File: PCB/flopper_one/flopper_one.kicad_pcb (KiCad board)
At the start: 2 copper layers, 76.8 x 63 mm, 23 parts, among them J1 To PN532 ->, J2 <- ST7789, Q1 2N2219, SW1 SW_Omron_B3FS, SW2 SW_Omron_B3FS, SW3 SW_Omron_B3FS, SW4 SW_Omron_B3FS, SW5 SW_Omron_B3FS, SW6 SW_SPST, U1 TP4056-42-ESOP8, U4 hw-045

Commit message: "quick" schematic fix
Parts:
- added R6: 0.4Ω, Resistor_THT:R_Axial_DIN0207_L6.3mm_D2.5mm_P7.62mm_Horizontal, F.Cu at (98.4, 33.5)
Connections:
- C2 pad 1: /VIN -> Net-(D2-A)
- D2 pad 2: GND -> Net-(D2-A)
- D3 pad 2: GND -> Net-(D2-A)
- U1 pad 4: /VIN -> Net-(D2-A)
- U1 pad 8: /VIN -> Net-(D2-A)
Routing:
- net Net-(D2-A): track 0.00 -> 100.2 mm, vias 0 -> 2
- net /VIN: track 71.0 -> 96.0 mm, vias 2 -> 3
- net GND: track 355.4 -> 343.3 mm

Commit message: flip r6
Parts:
- R6: moved to B.Cu
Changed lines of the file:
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@@
-		)
-	)
-	(footprint "Resistor_THT:R_Axial_DIN0207_L6.3mm_D2.5mm_P7.62mm_Horizontal"
-		(layer "F.Cu")
-		(at 98.38 33.5)
-		(descr "Resistor, Axial_DIN0207 series, Axial, Horizontal, pin pitch=7.62mm, 0.25W = 1/4W, length*diameter=6.3*2.5mm^2, http://cdn-reichelt.de/documents/datenblatt/B400/1_4W%23YAG.pdf")
-		(tags "Resistor Axial_DIN0207 series Axial Horizontal pin pitch 7.62mm 0.25W = 1/4W length 6.3mm diameter 2.5mm")
-		(property "Reference" "R6"
-			(at 3.81 -2.37 0)
-			(layer "F.SilkS")
-			(effects
-				(font
-					(size 1 1)
-					(thickness 0.15)
-				)
-			)
-		)
-		(property "Value" "0.4Ω"
-			(at 3.81 2.37 0)
-			(layer "F.Fab")
-			(effects
-				(font
-					(size 1 1)
-					(thickness 0.15)
-				)
-			)
-		)
-		(property "Datasheet" "~"
-			(at 0 0 0)
-			(layer "F.Fab")
-			(hide yes)
-			(effects
-				(font
-					(size 1.27 1.27)
-					(thickness 0.15)
-				)
-			)
-		)
-		(property "Description" "Resistor, US symbol"
-			(at 0 0 0)
-			(layer "F.Fab")
-			(hide yes)
-			(effects
-				(font
-					(size 1.27 1.27)
-					(thickness 0.15)
-				)
-			)
-		)
-		(property ki_fp_filters "R_*")
-		(sheetname "/")
-		(sheetfile "flopper_one.kicad_sch")
-		(attr through_hole)
-		(fp_line
-			(start 0.54 -1.37)
-			(end 7.08 -1.37)
-			(stroke
-				(width 0.12)
-				(type solid)
-			)
-			(layer "F.SilkS")
-		)
-		(fp_line
-			(start 0.54 -1.04)
-			(end 0.54 -1.37)
-			(stroke
-				(width 0.12)
-				(type solid)
-			)
-			(layer "F.SilkS")
-		)
-		(fp_line
-			(start 0.54 1.04)
-			(end 0.54 1.37)
-			(stroke
-				(width 0.12)
-				(type solid)
-			)
-			(layer "F.SilkS")
-		)
-		(fp_line
-			(start 0.54 1.37)
-			(end 7.08 1.37)
-			(stroke
-				(width 0.12)
-				(type solid)
-			)
-			(layer "F.SilkS")
-		)
-		(fp_line
-			(start 7.08 -1.37)
-			(end 7.08 -1.04)
-			(stroke
-				(width 0.12)
-				(type solid)
-			)
-			(layer "F.SilkS")
-		)
-		(fp_line
-			(start 7.08 1.37)
-			(end 7.08 1.04)
-			(stroke
-				(width 0.12)
-				(type solid)
-			)
-			(layer "F.SilkS")
-		)
-		(fp_rect
-			(start -1.05 -1.5)
-			(end 8.67 1.5)
-			(stroke
-				(width 0.05)
-				(type solid)
-			)
-			(fill no)
-			(layer "F.CrtYd")
-		)
-		(fp_line
-			(start 0 0)
-			(end 0.66 0)
-			(stroke
-				(width 0.1)
-				(type solid)
-			)
-			(layer "F.Fab")
-		)
-		(fp_line
-			(start 7.62 0)
-			(end 6.96 0)
-			(stroke
-				(width 0.1)
-				(type solid)
-			)
-			(layer "F.Fab")
-		)
-		(fp_rect
-			(start 0.66 -1.25)
-			(end 6.96 1.25)
-			(stroke
-				(width 0.1)
-				(type solid)
-			)
-			(fill no)
-			(layer "F.Fab")
-		)
-		(fp_text user "${REFERENCE}"
-			(at 3.81 0 0)
-			(layer "F.Fab")
-			(effects
-				(font
-					(size 1 1)
-					(thickness 0.15)
-				)
-			)
-		)
-		(pad "1" thru_hole circle
-			(at 0 0)
-			(size 1.6 1.6)
-			(drill 0.8)
-			(layers "*.Cu" "*.Mask")
-			(remove_unused_layers no)
-			(net 40 "/VIN")
-			(pintype "passive")
-		)
-		(pad "2" thru_hole circle
-			(at 7.62 0)
-			(size 1.6 1.6)
-			(drill 0.8)
-			(layers "*.Cu" "*.Mask")
-			(remove_unused_layers no)
-			(net 42 "Net-(D2-A)")
-			(pintype "passive")
-		)
-		(embedded_fonts no)
-		(model "${KICAD9_3DMODEL_DIR}/Resistor_THT.3dshapes/R_Axial_DIN0207_L6.3mm_D2.5mm_P7.62mm_Horizontal.step"
-			(offset
-				(xyz 0 0 0)
-			)
-			(scale
-				(xyz 1 1 1)
-			)
-			(rotate
-				(xyz 0 0 0)
-			)
 		)
 	)
@@
 			(offset
 				(xyz 0 0 0)
+			)
+			(scale
+				(xyz 1 1 1)
+			)
+			(rotate
+				(xyz 0 0 0)
+			)
+		)
+	)
+	(footprint "Resistor_THT:R_Axial_DIN0207_L6.3mm_D2.5mm_P7.62mm_Horizontal"
+		(layer "B.Cu")
+		(at 98.38 33.5)
+		(descr "Resistor, Axial_DIN0207 series, Axial, Horizontal, pin pitch=7.62mm, 0.25W = 1/4W, length*diameter=6.3*2.5mm^2, http://cdn-reichelt.de/documents/datenblatt/B400/1_4W%23YAG.pdf")
+		(tags "Resistor Axial_DIN0207 series Axial Horizontal pin pitch 7.62mm 0.25W = 1/4W length 6.3mm diameter 2.5mm")
+		(property "Reference" "R6"
+			(at 3.81 2.37 0)
+			(layer "B.SilkS")
+			(effects
+				(font
+					(size 1 1)
+					(thickness 0.15)
+				)
+				(justify mirror)
+			)
+		)
+		(property "Value" "0.4Ω"
+			(at 3.81 -2.37 0)
+			(layer "B.Fab")
+			(effects
+				(font
+					(size 1 1)
+					(thickness 0.15)
+				)
+				(justify mirror)
+			)
+		)
+		(property "Datasheet" "~"
+			(at 0 0 0)
+			(layer "B.Fab")
+			(hide yes)
+			(effects
+				(font
+					(size 1.27 1.27)
+					(thickness 0.15)
+				)
+				(justify mirror)
+			)
+		)
+		(property "Description" "Resistor, US symbol"
+			(at 0 0 0)
+			(layer "B.Fab")
+			(hide yes)
+			(effects
+				(font
+					(size 1.27 1.27)
+					(thickness 0.15)
+				)
+				(justify mirror)
+			)
+		)
+		(property ki_fp_filters "R_*")
+		(sheetname "/")
+		(sheetfile "flopper_one.kicad_sch")
+		(attr through_hole)
+		(fp_line
+			(start 0.54 -1.37)
+			(end 7.08 -1.37)
+			(stroke
+				(width 0.12)
+				(type solid)
+			)
+			(layer "B.SilkS")
+		)
+		(fp_line
+			(start 0.54 -1.04)
+			(end 0.54 -1.37)
+			(stroke
+				(width 0.12)
+				(type solid)
+			)
+			(layer "B.SilkS")
+		)
+		(fp_line
+			(start 0.54 1.04)
+			(end 0.54 1.37)
+			(stroke
+				(width 0.12)
+				(type solid)
+			)
+			(layer "B.SilkS")
+		)
+		(fp_line
+			(start 0.54 1.37)
+			(end 7.08 1.37)
+			(stroke
+				(width 0.12)
+				(type solid)
+			)
+			(layer "B.SilkS")
+		)
+		(fp_line
+			(start 7.08 -1.37)
+			(end 7.08 -1.04)
+			(stroke
+				(width 0.12)
+				(type solid)
+			)
+			(layer "B.SilkS")
+		)
+		(fp_line
+			(start 7.08 1.37)
+			(end 7.08 1.04)
+			(stroke
+				(width 0.12)
+				(type solid)
+			)
+			(layer "B.SilkS")
+		)
+		(fp_rect
+			(start -1.05 1.5)
+			(end 8.67 -1.5)
+			(stroke
+				(width 0.05)
+				(type solid)
+			)
+			(fill no)
+			(layer "B.CrtYd")
+		)
+		(fp_line
+			(start 0 0)
+			(end 0.66 0)
+			(stroke
+				(width 0.1)
+				(type solid)
+			)
+			(layer "B.Fab")
+		)
+		(fp_line
+			(start 7.62 0)
+			(end 6.96 0)
+			(stroke
+				(width 0.1)
+				(type solid)
+			)
+			(layer "B.Fab")
+		)
+		(fp_rect
+			(start 0.66 1.25)
+			(end 6.96 -1.25)
+			(stroke
+				(width 0.1)
+				(type solid)
+			)
+			(fill no)
+			(layer "B.Fab")
+		)
+		(fp_text user "${REFERENCE}"
+			(at 3.81 0 0)
+			(layer "B.Fab")
+			(effects
+				(font
+					(size 1 1)
+					(thickness 0.15)
+				)
+				(justify mirror)
+			)
+		)
+		(pad "1" thru_hole circle
+			(at 0 0)
+			(size 1.6 1.6)
+			(drill 0.8)
+			(layers "*.Cu" "*.Mask")
+			(remove_unused_layers no)
+			(net 40 "/VIN")
+			(pintype "passive")
+		)
+		(pad "2" thru_hole circle
+			(at 7.62 0)
+			(size 1.6 1.6)
+			(drill 0.8)
+			(layers "*.Cu" "*.Mask")
+			(remove_unused_layers no)
+			(net 42 "Net-(D2-A)")
+			(pintype "passive")
+		)
+		(embedded_fonts no)
+		(model "${KICAD9_3DMODEL_DIR}/Resistor_THT.3dshapes/R_Axial_DIN0207_L6.3mm_D2.5mm_P7.62mm_Horizontal.step"
+			(offset
+				(xyz 0 0 0)

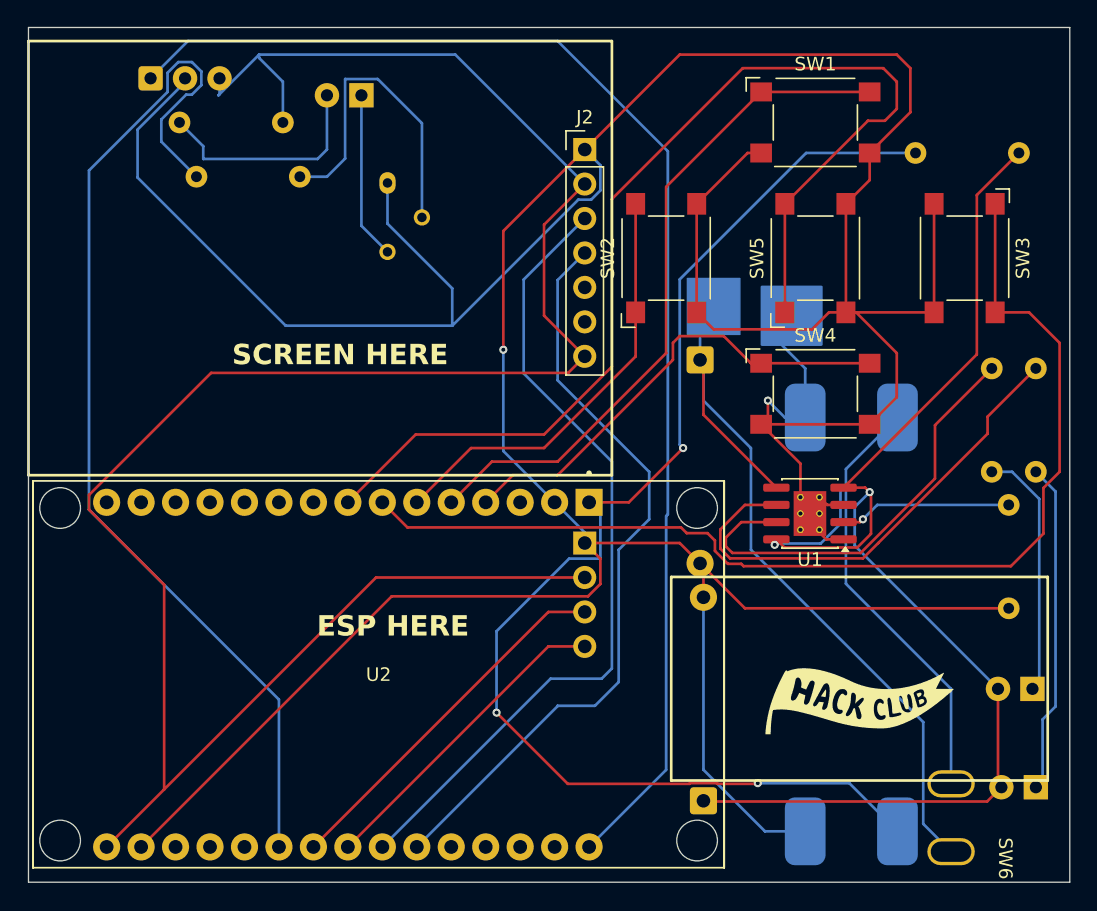
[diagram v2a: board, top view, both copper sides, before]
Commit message: make thicker and add gnd pour
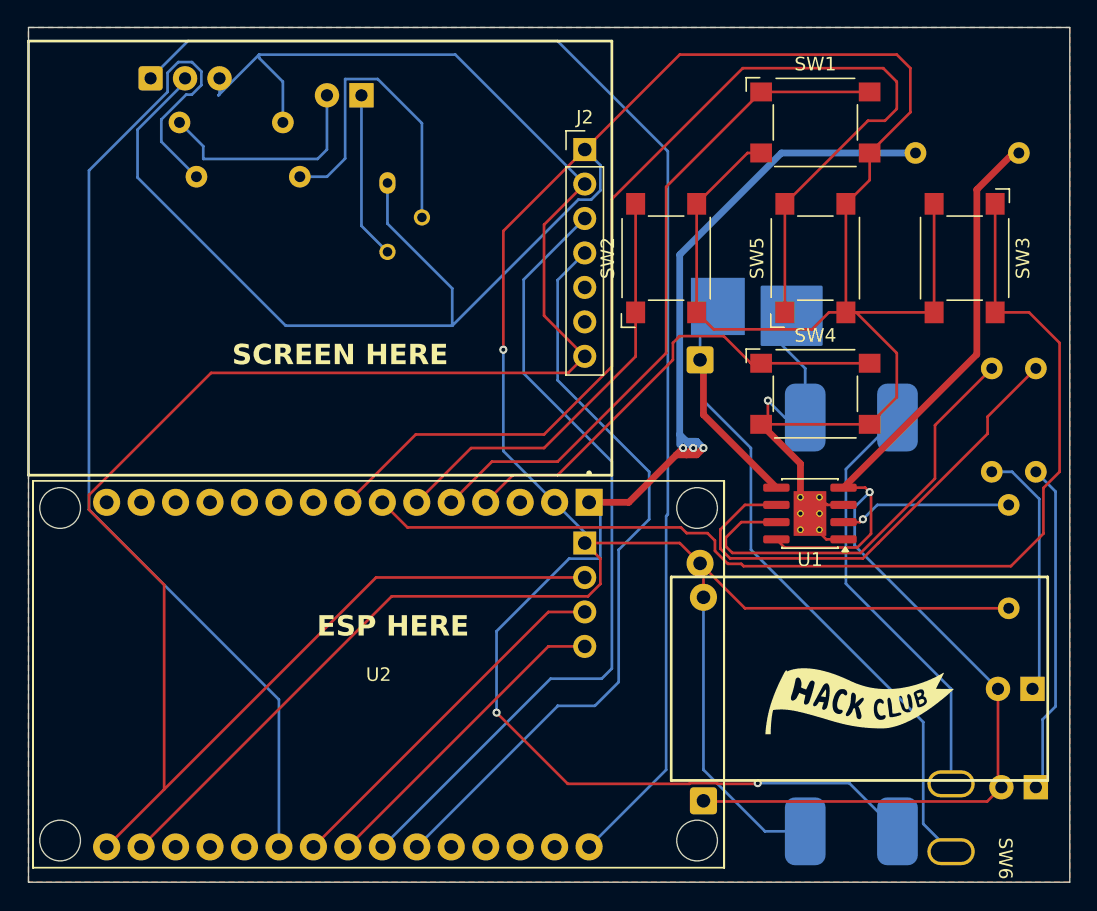
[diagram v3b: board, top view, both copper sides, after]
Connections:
- net Net-(D2-A) renamed /CE
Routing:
- net /CE: track 100.2 -> 92.2 mm, vias 2 -> 1
- net /VIN: track 96.0 -> 102.8 mm, vias 3 -> 5
- added copper zone on B.Cu, net GND
- added copper zone on F.Cu, net GND
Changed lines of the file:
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@@
 	(net 40 "/VIN")
 	(net 41 "Net-(SW6-A)")
-	(net 42 "Net-(D2-A)")
+	(net 42 "/CE")
 	(footprint "wroom:MODULE_DEVKIT_V1_ESP32-WROOM-32"
 		(layer "F.Cu")
@@
 			(layers "F.Cu" "F.Mask" "F.Paste")
 			(roundrect_rratio 0.25)
-			(net 42 "Net-(D2-A)")
+			(net 42 "/CE")
 			(pinfunction "V_{CC}")
 			(pintype "power_in")
@@
 			(layers "F.Cu" "F.Mask" "F.Paste")
 			(roundrect_rratio 0.25)
-			(net 42 "Net-(D2-A)")
+			(net 42 "/CE")
 			(pinfunction "CE")
 			(pintype "input")
@@
 			(layers "*.Cu" "*.Mask")
 			(remove_unused_layers no)
-			(net 42 "Net-(D2-A)")
+			(net 42 "/CE")
 			(pinfunction "A")
 			(pintype "passive")
@@
 			(layers "*.Cu" "*.Mask")
 			(remove_unused_layers no)
-			(net 42 "Net-(D2-A)")
+			(net 42 "/CE")
 			(pintype "passive")
 		)
@@
 			(remove_unused_layers no)
 			(roundrect_rratio 0.125)
-			(net 42 "Net-(D2-A)")
+			(net 42 "/CE")
 			(pintype "passive")
 		)
@@
 			(layers "*.Cu" "*.Mask")
 			(remove_unused_layers no)
-			(net 42 "Net-(D2-A)")
+			(net 42 "/CE")
 			(pinfunction "A")
 			(pintype "passive")
@@
 	)
 	(gr_rect
-		(start 81.5625 42.75)
-		(end 85.4375 46.875)
+		(start 81.875 42.75)
+		(end 85.75 46.875)
 		(stroke
 			(width 0.1)
@@
 	)
 	(gr_rect
-		(start 81.625 42.625)
-		(end 85.5 46.75)
+		(start 81.9375 42.625)
+		(end 85.8125 46.75)
 		(stroke
 			(width 0.1)
@@
 		(start 89.9 58.875)
 		(end 89.9 56.4)
-		(width 0.2)
+		(width 0.5)
 		(layer "F.Cu")
 		(net 3)
@@
 		(start 89.9 56.4)
 		(end 87 53.5)
-		(width 0.2)
+		(width 0.5)
 		(layer "F.Cu")
 		(net 3)
@@
 		(start 88.125 58.17)
 		(end 82.75 52.795)
-		(width 0.2)
+		(width 0.5)
 		(layer "F.Cu")
 		(net 39)
@@
 		(start 82.75 52.795)
 		(end 82.75 49)
-		(width 0.2)
+		(width 0.5)
 		(layer "F.Cu")
 		(net 39)
@@
 		(start 77.25 59.25)
 		(end 74.32 59.25)
-		(width 0.2)
+		(width 0.5)
+		(layer "F.Cu")
+		(net 40)
+	)
+	(segment
+		(start 81.25 55.25)
+		(end 80.75 55.75)
+		(width 0.5)
+		(layer "F.Cu")
+		(net 40)
+	)
+	(segment
+		(start 81.5 55.75)
+		(end 82.25 55.75)
+		(width 0.5)
+		(layer "F.Cu")
+		(net 40)
+	)
+	(segment
+		(start 80.75 55.75)
+		(end 81.5 55.75)
+		(width 0.5)
 		(layer "F.Cu")
 		(net 40)
@@
 	)
 	(segment
-		(start 81.25 55.25)
+		(start 80.75 55.75)
 		(end 77.25 59.25)
-		(width 0.2)
+		(width 0.5)
+		(layer "F.Cu")
+		(net 40)
+	)
+	(segment
+		(start 81.5 55.75)
+		(end 82 55.25)
+		(width 0.5)
 		(layer "F.Cu")
 		(net 40)
@@
 		(net 40)
 	)
+	(segment
+		(start 82.25 55.75)
+		(end 82.75 55.25)
+		(width 0.5)
+		(layer "F.Cu")
+		(net 40)
+	)
 	(via
 		(at 86.75 79.949)
@@
 	)
 	(via
+		(at 82.75 55.25)
+		(size 0.6)
+		(drill 0.3)
+		(layers "F.Cu" "B.Cu")
+		(net 40)
+	)
+	(via
 		(at 67.5 74.75)
 		(size 0.6)
@@
 		(net 40)
 	)
+	(via
+		(at 82 55.25)
+		(size 0.6)
+		(drill 0.3)
+		(layers "F.Cu" "B.Cu")
+		(net 40)
+	)
+	(segment
+		(start 88.5 33.5)
+		(end 98.38 33.5)
+		(width 0.5)
+		(layer "B.Cu")
+		(net 40)
+	)
+	(segment
+		(start 81 54.25)
+		(end 81 41)
+		(width 0.5)
+		(layer "B.Cu")
+		(net 40)
+	)
+	(segment
+		(start 81 41)
+		(end 88.5 33.5)
+		(width 0.5)
+		(layer "B.Cu")
+		(net 40)
+	)
+	(segment
+		(start 81.5 54.75)
+		(end 81 54.25)
+		(width 0.5)
+		(layer "B.Cu")
+		(net 40)
+	)
 	(segment
 		(start 81 55)
@@
 	)
 	(segment
+		(start 82.75 55.25)
+		(end 82.25 54.75)
+		(width 0.5)
+		(layer "B.Cu")
+		(net 40)
+	)
+	(segment
 		(start 75.151 60.081)
 		(end 74.32 59.25)
@@
 	)
 	(segment
-		(start 98.38 33.5)
-		(end 90.316111 33.5)
-		(width 0.2)
+		(start 82 55.25)
+		(end 81.5 54.75)
+		(width 0.5)
 		(layer "B.Cu")
 		(net 40)
 	)
 	(segment
-		(start 90.316111 33.5)
-		(end 81 42.816111)
-		(width 0.2)
+		(start 82.25 54.75)
+		(end 81.5 54.75)
+		(width 0.5)
 		(layer "B.Cu")
 		(net 40)
 	)
 	(segment
-		(start 81 42.816111)
-		(end 81 55)
-		(width 0.2)
+		(start 81 55)
+		(end 81 54.25)
+		(width 0.5)
 		(layer "B.Cu")
 		(net 40)
@@
 	)
 	(segment
-		(start 88.125 62.257)
-		(end 88 62.382)
+		(start 95.101 61.570968)
+		(end 94.090968 62.581)
 		(width 0.2)
 		(layer "F.Cu")
@@
 	)
 	(segment
-		(start 88.125 61.98)
-		(end 88.125 62.257)
-		(width 0.2)
+		(start 102.899 36.199)
+		(end 105.598 33.5)
+		(width 0.5)
 		(layer "F.Cu")
 		(net 42)
 	)
 	(segment
-		(start 95.101 61.570968)
-		(end 94.090968 62.581)
-		(width 0.2)
+		(start 93.075 58.17)
+		(end 102.899 48.346)
+		(width 0.5)
 		(layer "F.Cu")
 		(net 42)
 	)
 	(segment
-		(start 95.101 58.601)
-		(end 95.101 61.570968)
-		(width 0.2)
+		(start 105.598 33.5)
+		(end 106 33.5)
+		(width 0.5)
 		(layer "F.Cu")
 		(net 42)
 	)
 	(segment
-		(start 102.899 48.346)
-		(end 93.075 58.17)
+		(start 95.101 58.601)
+		(end 95.101 61.570968)
 		(width 0.2)
 		(layer "F.Cu")
@@
 	)
 	(segment
-		(start 106 33.5)
-		(end 102.899 36.601)
-		(width 0.2)
-		(layer "F.Cu")
-		(net 42)
-	)
-	(segment
-		(start 102.899 36.601)
-		(end 102.899 48.346)
-		(width 0.2)
-		(layer "F.Cu")
-		(net 42)
-	)
-	(segment
 		(start 94.67 58.17)
 		(end 93.075 58.17)
@@
 	)
 	(segment
+		(start 102.899 48.346)
+		(end 102.899 36.199)
+		(width 0.5)
+		(layer "F.Cu")
+		(net 42)
+	)
+	(segment
 		(start 104.46 73)
 		(end 104.46 80)
@@
 	)
 	(via
-		(at 88 62.382)
-		(size 0.6)
-		(drill 0.3)
-		(layers "F.Cu" "B.Cu")
-		(net 42)
-	)
-	(via
 		(at 95 58.5)
 		(size 0.6)
@@
 	)
 	(segment
-		(start 88.09566 62.28634)
-		(end 91.39066 62.28634)
-		(width 0.2)
-		(layer "B.Cu")
-		(net 42)
-	)
-	(segment
 		(start 93.899 59.601)
 		(end 95 58.5)
@@
 	)
 	(segment
-		(start 91.39066 62.28634)
-		(end 92.849 60.828)
-		(width 0.2)
-		(layer "B.Cu")
-		(net 42)
-	)
-	(segment
-		(start 88 62.382)
-		(end 88.09566 62.28634)
-		(width 0.2)
-		(layer "B.Cu")
-		(net 42)
-	)
-	(segment
 		(start 104.46 73)
 		(end 93.899 62.439)
@@
 		(net 42)
 	)
-	(segment
-		(start 92.849 60.828)
-		(end 92.849 58.5)
-		(width 0.2)
+	(zone
+		(net 3)
+		(net_name "GND")
+		(layer "F.Cu")
+		(hatch edge 0.5)
+		(connect_pads
+			(clearance 0.5)
+		)
+		(min_thickness 0.25)
+		(filled_areas_thickness no)
+		(fill yes
+			(thermal_gap 0.5)
+			(thermal_bridge_width 0.5)
+		)
+		(polygon
+			(pts
+				(xy 33 24.25) (xy 109.75 24.25) (xy 109.75 87.25) (xy 33 87.25)
+			)
+		)
+	)
+	(zone
+		(net 3)
+		(net_name "GND")
 		(layer "B.Cu")
-		(net 42)
+		(hatch edge 0.5)
+		(priority 1)
+		(connect_pads
+			(clearance 0.5)
+		)
+		(min_thickness 0.25)
+		(filled_areas_thickness no)
+		(fill yes
+			(thermal_gap 0.5)
+			(thermal_bridge_width 0.5)
+		)
+		(polygon
+			(pts
+				(xy 33 24.25) (xy 109.75 24.25) (xy 109.75 87.25) (xy 33 87.25)
+			)
+		)
 	)
 	(group ""

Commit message: adfadfds
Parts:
- removed R6: 0.4Ω, Resistor_THT:R_Axial_DIN0207_L6.3mm_D2.5mm_P7.62mm_Horizontal
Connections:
- U2 pad 1: /VIN -> /CE
- U4 pad 1: /VIN -> /CE
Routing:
- net /VIN: track 102.8 -> 0.00 mm, vias 5 -> 0
- net /CE: track 92.2 -> 167.2 mm, vias 1 -> 3
- net GND: track 343.3 -> 373.3 mm
- net /P4: track 34.9 -> 36.6 mm
- net /P1: track 50.5 -> 49.8 mm
